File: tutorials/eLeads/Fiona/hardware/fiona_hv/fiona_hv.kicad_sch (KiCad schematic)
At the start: 36 parts, among them SW101 SW_SPDT, SW102 SW_SPDT, U101 OpAmp, U102 ATMEGA16M1, U103 OpAmp, U104 LM397, U105 MCP2561-E_SN, U106 AD8494, Y101 Crystal_16MHz_18pF

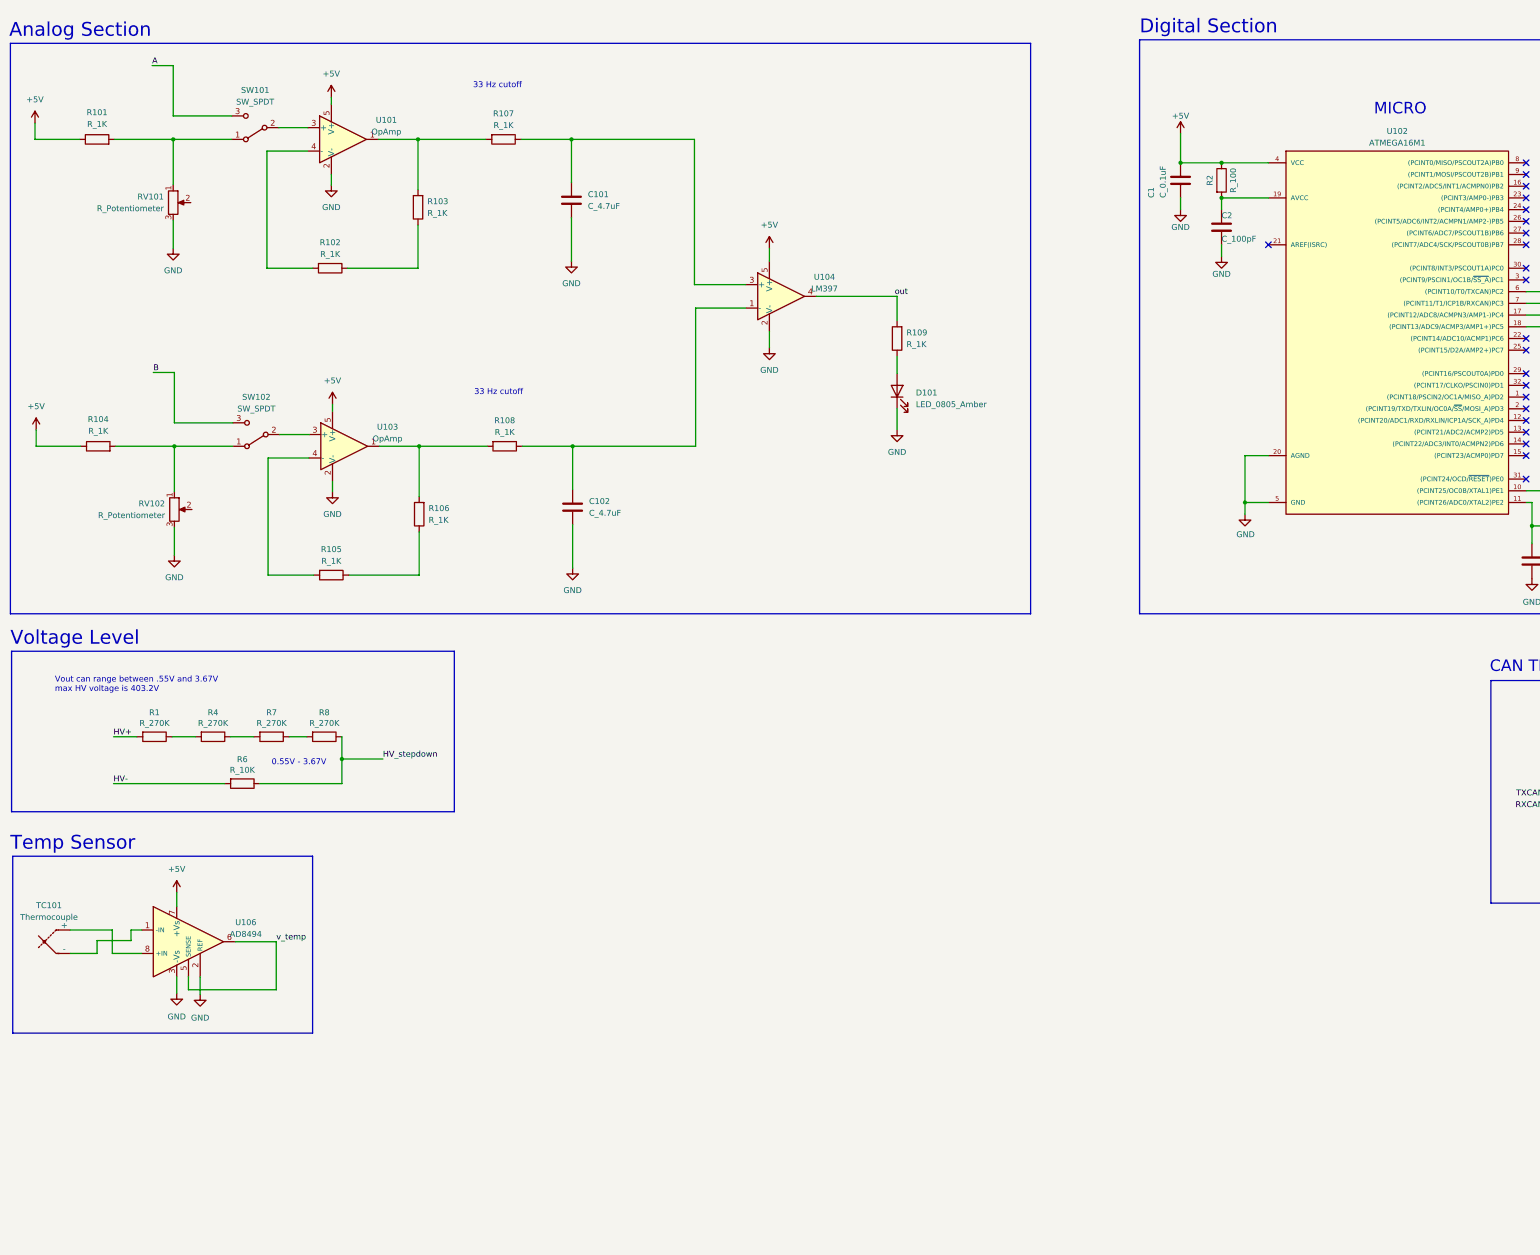
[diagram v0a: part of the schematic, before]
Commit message: Add test points and status LEDs
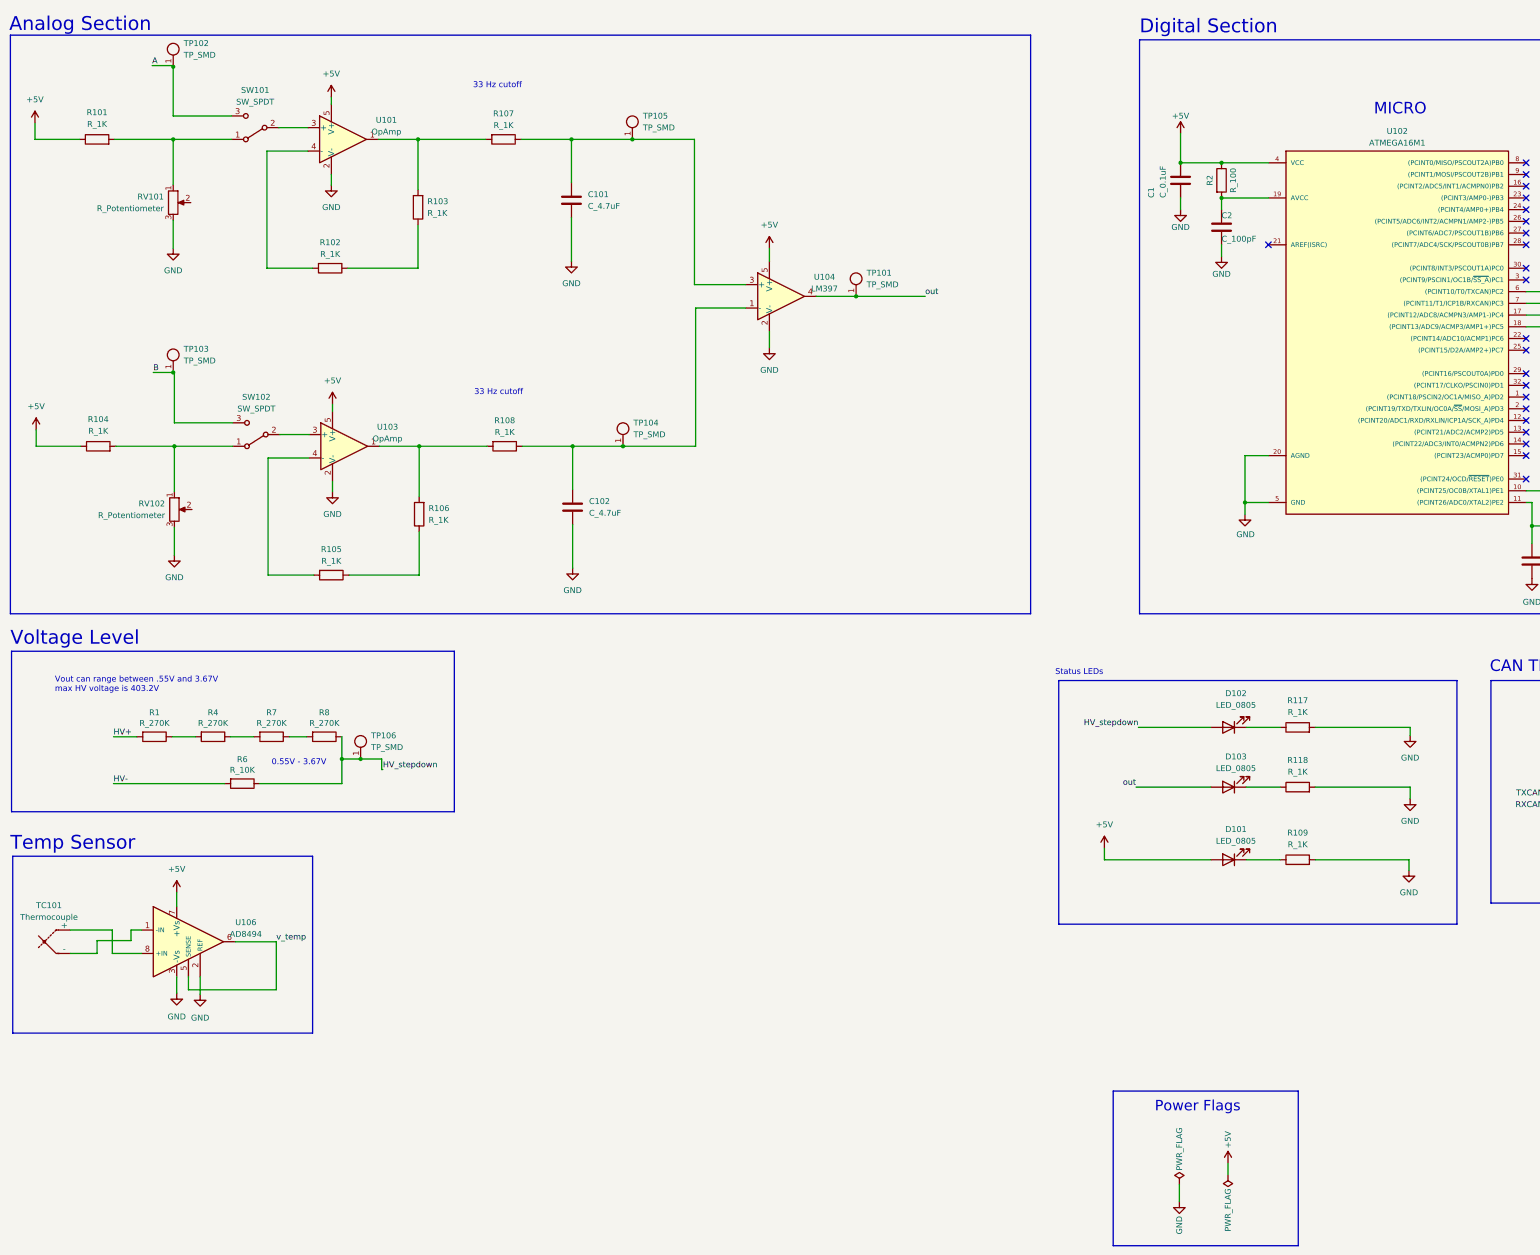
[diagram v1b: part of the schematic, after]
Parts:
- removed D101: LED_0805_Amber, footprints:LED_0805_OEM, symbol formula:LED_0805_Amber
- added D101, D102, D103: LED_0805, footprints:LED_0805_OEM, symbol formula:LED_0805
- added R117, R118: R_1K, OEM:R_0603, symbol formula:R_1K
- added TP101, TP102, TP103, TP104, TP105, TP106: TP_SMD, footprints:Test_Point_SMD, symbol formula:TP_SMD
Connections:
- net +5V: now also D101.2 (A)
- net A: now also TP102.1
- net B: now also TP103.1
- net GND: now also R109.2, R117.2, R118.2
- net HV_stepdown: now also D102.2 (A), TP106.1
- net out: now also D103.2 (A), TP101.1; no longer R109.2
- net at R109.1: now also D101.1 (K)
- net at C102.1, R108.1, U104.1 (-): now also TP104.1
- net at C101.1, R107.1, U104.3 (+): now also TP105.1
- new net: D102.1 (K), R117.1
- new net: D103.1 (K), R118.1
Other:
- note added: "Power Flags"
- note added: "Status LEDs"

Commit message: Add relays and HV buffer
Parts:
- added D2 (x2): SMBJ5355B-TP, footprints:DO-214AA, symbol OEM:SMBJ5355B-TP
- added J101, J102: MicroFit_VT_4, footprints:MicroFit_VT_4, symbol formula:MicroFit_VT_4
- added K1 (x2): G5Q-1A4-DC5, footprints:Relay_SPST_OMRON-G5Q-1A4_OEM, symbol OEM:G5Q-1A4-DC5
- added Q2 (x2): SSM3K333R, OEM:SOT-23F, symbol OEM:SSM3K333R
- added R119, R120, R121, R122: R_1M, footprints:R_0805_OEM, symbol formula:R_1M
- added TP107, TP108: TP_SMD, footprints:Test_Point_SMD, symbol formula:TP_SMD
- added TP5 (x2): BSPD, footprints:Test_Point_SMD, symbol OEM:TP_SMD
- added U107: OpAmp, OEM:SOT-23-5, symbol OEM:OpAmp
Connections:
- net +5V: now also D2.1 (K), D2.1 (K), K1.5, K1.5, U107.5 (V+)
- net A: now also J102.3, R119.1
- net B: now also J102.4, R120.1
- net GND: now also J101.2, Q2.2 (S), Q2.2 (S), R119.2, R120.2, R122.1, U107.2 (V-)
- net HV-: now also R122.2
- net HV_stepdown: now also TP107.1, U107.1, U107.4 (-); no longer R6.1, R8.1, TP106.1
- net v_temp: now also Q2.1 (G), TP108.1, TP5.1
- net out renamed analog_out
- net analog_out: now also Q2.1 (G), TP5.1
- new net: R121.1, R6.1, R8.1
- new net: D2.2 (A), K1.1, Q2.3 (D) (x2)
- new net: K1.2, K1.3
- new net: R121.2, TP106.1, U107.3 (+)
- new net +5: J101.1
- new net CAN+: J101.3
- new net CAN-: J101.4
- new net SHUTDOWN_IN: J102.1, K1.3
- new net SHUTDOWN_OUT: J102.2, K1.2
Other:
- note added: "Connectors"
- note added: "Relays"
- moved on the sheet: C1, D101, D102, D103, R109, R111, R117, R118, TC101, TP106, U105, U106
